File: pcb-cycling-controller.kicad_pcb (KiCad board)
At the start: 4 copper layers, 54.6 x 40.6 mm, 85 parts, among them J1 Conn_01x02, J2 USB_C_Receptacle_USB2.0_16P, J3 Conn_01x06, J6 LED1, J7 LED1, Q1 SI2301CDS-T1-GE3-ES, Q2 SI2301CDS-T1-GE3-ES, SW1 SS12F44G4, U1 ESP32-S3-WROOM-1, U2 LMV321, U3 L7805, U4 MT3410LB, U5 74AHCT125, U7 DS1307Z+, U8 LMV321, Y2 32.768 kHz

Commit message: Add details to the design
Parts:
- removed C32: 0.1uF, Capacitor_SMD:C_0402_1005Metric
- removed R14, R15, R37: 0, Resistor_SMD:R_0603_1608Metric
- removed R32: 11k, Resistor_SMD:R_0603_1608Metric
- removed R33: 3.3k, Resistor_SMD:R_0603_1608Metric
- removed U8: LMV321, Package_TO_SOT_SMD:SOT-23-5_HandSoldering
- added C34: 0.1uF, Capacitor_SMD:C_0402_1005Metric, B.Cu at (70.1, 94.7)
- added C35: 0.1uF, Capacitor_SMD:C_0402_1005Metric, F.Cu at (82.8, 90.4)
- added C36: 0.1uF, Capacitor_SMD:C_0402_1005Metric, F.Cu at (84.6, 90.4)
- added C9: 1uF, Capacitor_SMD:C_0603_1608Metric, B.Cu at (75.7, 84.8)
- added D8: A7, Diode_SMD:D_SOD-123F, F.Cu at (75.9, 77.0)
- added J8: SENSOR, Connector_Molex:Molex_KK-254_AE-6410-03A_1x03_P2.54mm_Vertical, F.Cu at (63.2, 82.5)
- added J9: OLED, Connector_PinSocket_2.54mm:PinSocket_1x04_P2.54mm_Vertical, F.Cu at (78.0, 105.4)
- added R38: 0, Resistor_SMD:R_0603_1608Metric, F.Cu at (67.6, 95.5)
- added R39: 0, Resistor_SMD:R_0603_1608Metric, B.Cu at (70.6, 96.8)
- added R40: 0, Resistor_SMD:R_0603_1608Metric, F.Cu at (67.6, 98.6)
- added R5: 10k, Resistor_SMD:R_0603_1608Metric, F.Cu at (82.8, 87.9)
- added R6: 10k, Resistor_SMD:R_0603_1608Metric, F.Cu at (84.6, 87.9)
- added SW2: BTN1, jlcpcb:SW-SMD_4P-L5.1-W5.1-P3.70-LS6.5-TL_H1.5, F.Cu at (78.2, 90.7)
- added SW3: BTN2, jlcpcb:SW-SMD_4P-L5.1-W5.1-P3.70-LS6.5-TL_H1.5, F.Cu at (89.2, 90.7)
- added U6: AMS1117-5.0, Package_TO_SOT_SMD:SOT-223-3_TabPin2, B.Cu at (70.6, 88.1)
- C33: value 0.1uF -> 22uF 10V; footprint Capacitor_SMD:C_0402_1005Metric -> Capacitor_SMD:C_0603_1608Metric; moved to B.Cu
- J1: value Conn_01x02 -> Power; footprint Connector_PinHeader_2.54mm:PinHeader_1x02_P2.54mm_Vertical -> Connector_Molex:Molex_KK-254_AE-6410-02A_1x02_P2.54mm_Vertical
- J2: value USB_C_Receptacle_USB2.0_16P -> USB
- J3: value Conn_01x06 -> PROG
- J6: footprint Connector_PinHeader_2.54mm:PinHeader_1x05_P2.54mm_Vertical -> Connector_Molex:Molex_KK-254_AE-6410-04A_1x04_P2.54mm_Vertical
- J7: value LED1 -> LED2; footprint Connector_PinHeader_2.54mm:PinHeader_1x05_P2.54mm_Vertical -> Connector_Molex:Molex_KK-254_AE-6410-04A_1x04_P2.54mm_Vertical
- U3: value L7805 -> AMS1117-5.0; footprint Package_TO_SOT_SMD:TO-263-2 -> Package_TO_SOT_SMD:SOT-223-3_TabPin2
- U5: footprint Package_SO:SOIC-14W_7.5x9mm_P1.27mm -> Package_SO:TSSOP-14_4.4x5mm_P0.65mm
- moved C28 72.8 mm to (82.3, 100.1), turned to -90 degrees
- moved FID1 70.9 mm to (107.4, 69.6)
- moved R31 70.1 mm to (70.4, 81.0)
- moved R18 69.6 mm to (82.3, 102.9)
- moved R12 68.3 mm to (86.4, 102.9), turned to 180 degrees
- moved R19 67.5 mm to (80.8, 100.1), turned to 90 degrees
- moved C31 67.0 mm to (73.9, 77.0), turned to 90 degrees
- moved C33 65.5 mm to (69.8, 93.5)
- moved U2 62.7 mm to (70.9, 78.4)
- moved R20 62.1 mm to (67.6, 78.5), turned to 90 degrees
- moved C30 62.1 mm to (73.7, 82.3), turned to 180 degrees
- moved C29 62.0 mm to (83.6, 99.5), turned to -90 degrees
- moved R13 61.8 mm to (70.4, 75.7)
- moved R21 61.0 mm to (73.4, 81.0)
- moved D7 60.1 mm to (79.0, 100.1), turned to -90 degrees
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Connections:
- net /BUCK_VIN renamed BUCK_VIN
- C14 pad 2: +5V -> Net-(U3-VO)
- C15 pad 1: +5V -> Net-(U3-VO)
- C30 pad 1: SENSOR_1_FILT -> SENSOR_FILT
- C33 pad 1: SENSOR_1_FILT -> GND
- C33 pad 2: GND -> Net-(U6-VO)
- J6 pad 1: VLED -> VLED1
- J6 pad 4: SENSOR_1 -> GND
- J7 pad 1: VLED -> VLED2
- J7 pad 4: SENSOR_2 -> GND
- R20 pad 1: SENSOR_1 -> Net-(J8-Pin_2)
- R21 pad 1: Net-(U2--) -> Net-(R21-Pad1)
- R21 pad 2: SENSOR_1_FILT -> SENSOR_FILT
- R31 pad 1: SENSOR_1 -> Net-(U2--)
- R31 pad 2: Net-(U8-+) -> Net-(R21-Pad1)
- U1 pad 10: STATUS -> unconnected-(U1-IO17-Pad10)
- U1 pad 15: unconnected-(U1-IO3-Pad15) -> BATT_VOLTAGE
- U1 pad 16: unconnected-(U1-IO46-Pad16) -> STATUS
- U1 pad 17: unconnected-(U1-IO9-Pad17) -> SENSOR_FILT
- U1 pad 18: unconnected-(U1-IO10-Pad18) -> BTN1
- U1 pad 19: unconnected-(U1-IO11-Pad19) -> BTN2
- U1 pad 25: unconnected-(U1-IO48-Pad25) -> I2C_SDA
- U1 pad 26: unconnected-(U1-IO45-Pad26) -> I2C_SCL
- U1 pad 31: STRIP1_D -> STRIP2_C
- U1 pad 32: STRIP1_C -> STRIP2_D
- U1 pad 33: STRIP2_D -> STRIP1_C
- U1 pad 34: STRIP2_C -> STRIP1_D
- U1 pad 39: BATT_VOLTAGE -> unconnected-(U1-IO1-Pad39)
- U1 pad 4: I2C_SDA -> unconnected-(U1-IO4-Pad4)
- U1 pad 5: I2C_SCL -> unconnected-(U1-IO5-Pad5)
- U1 pad 6: SENSOR1_FILT -> unconnected-(U1-IO6-Pad6)
- U1 pad 7: SENSOR2_FILT -> unconnected-(U1-IO7-Pad7)
- U2 pad 4: Net-(U2--) -> Net-(R21-Pad1)
- U3 pad 1: VBAT_SW -> GND
- U3 pad 2: GND -> Net-(U3-VO)
- U3 pad 3: +5V -> VBAT_SW
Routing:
- net ~{RST}: track 0.00 -> 45.2 mm, vias 0 -> 1
- net VBAT_PROT: track 11.4 -> 54.8 mm, vias 0 -> 1
- net GND: track 35.4 -> 73.2 mm, vias 22 -> 68
- net STRIP1_C: track 0.00 -> 35.9 mm, vias 0 -> 2
- net STRIP2_D: track 0.00 -> 35.3 mm, vias 0 -> 2
- net STRIP1_D: track 0.00 -> 35.2 mm, vias 0 -> 2
- net Net-(D8-A): track 0.00 -> 30.3 mm, vias 0 -> 3
- net STRIP2_C: track 0.00 -> 30.1 mm, vias 0 -> 2
- net +3V3: track 5.55 -> 28.1 mm, vias 0 -> 19
- net SENSOR_FILT: track 0.00 -> 22.5 mm, vias 0 -> 2
- net BTN1: track 0.00 -> 21.2 mm
- net Net-(J2-SHIELD): track 0.00 -> 19.0 mm
- net I2C_SCL: track 0.00 -> 16.9 mm, vias 0 -> 2
- net I2C_SDA: track 0.00 -> 16.4 mm
- net VLED2: track 0.00 -> 15.4 mm, vias 0 -> 2
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- added copper zone on In2.Cu, net +3V3
- added copper zone on F.Cu, net GND
- added copper zone on In2.Cu, net VBAT_SW
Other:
- board text removed: "SCL"
- board text removed: "SDA"

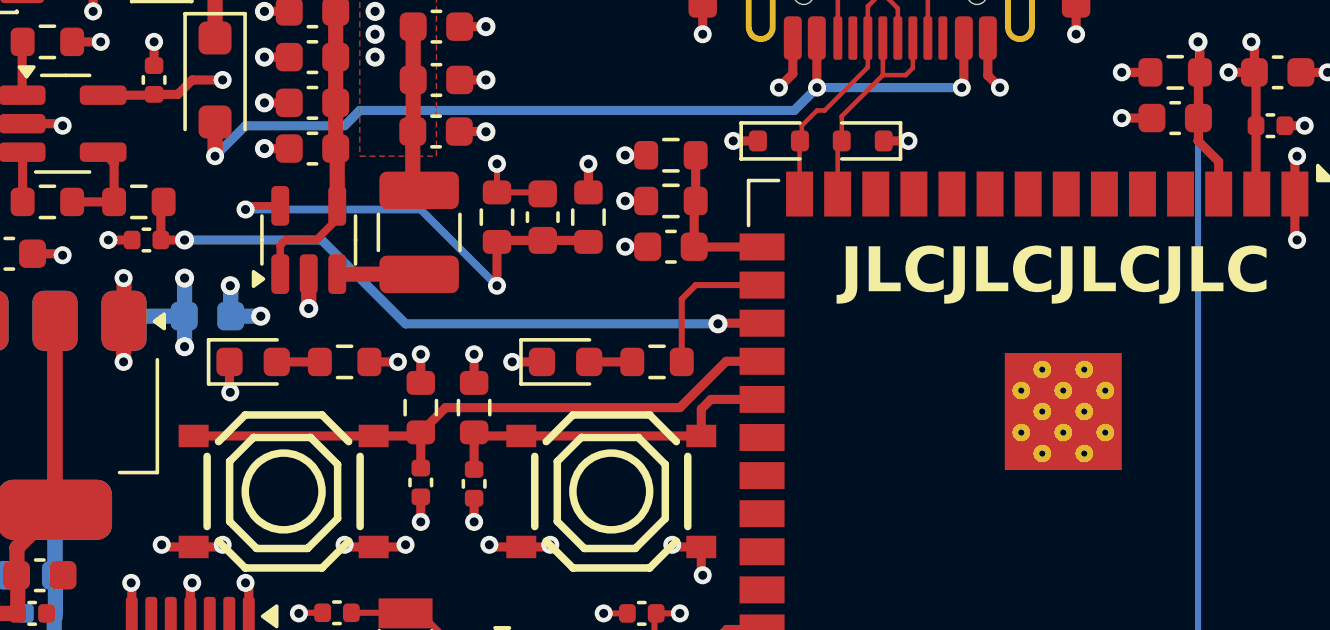
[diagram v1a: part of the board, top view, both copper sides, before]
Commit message: Update ADC pin assignments due to issue #4
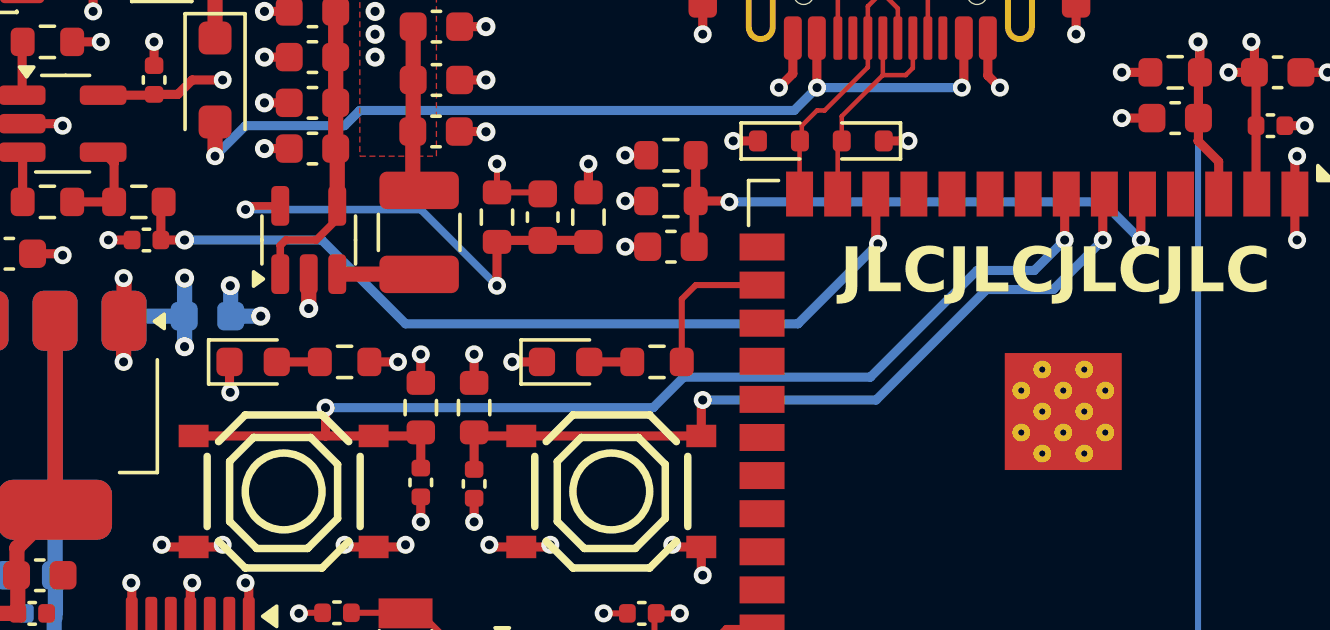
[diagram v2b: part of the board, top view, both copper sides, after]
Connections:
- U1 pad 12: unconnected-(U1-IO8-Pad12) -> SENSOR_FILT
- U1 pad 15: BATT_VOLTAGE -> unconnected-(U1-IO3-Pad15)
- U1 pad 17: SENSOR_FILT -> unconnected-(U1-IO9-Pad17)
- U1 pad 18: BTN1 -> unconnected-(U1-IO10-Pad18)
- U1 pad 19: BTN2 -> unconnected-(U1-IO11-Pad19)
- U1 pad 5: unconnected-(U1-IO5-Pad5) -> BATT_VOLTAGE
- U1 pad 6: unconnected-(U1-IO6-Pad6) -> BTN2
- U1 pad 7: unconnected-(U1-IO7-Pad7) -> BTN1
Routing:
- net BTN1: track 21.2 -> 38.3 mm, vias 0 -> 2
- net BTN2: track 11.9 -> 27.2 mm, vias 0 -> 2
- net BATT_VOLTAGE: track 5.42 -> 20.1 mm, vias 0 -> 2
- net SENSOR_FILT: track 22.5 -> 29.2 mm

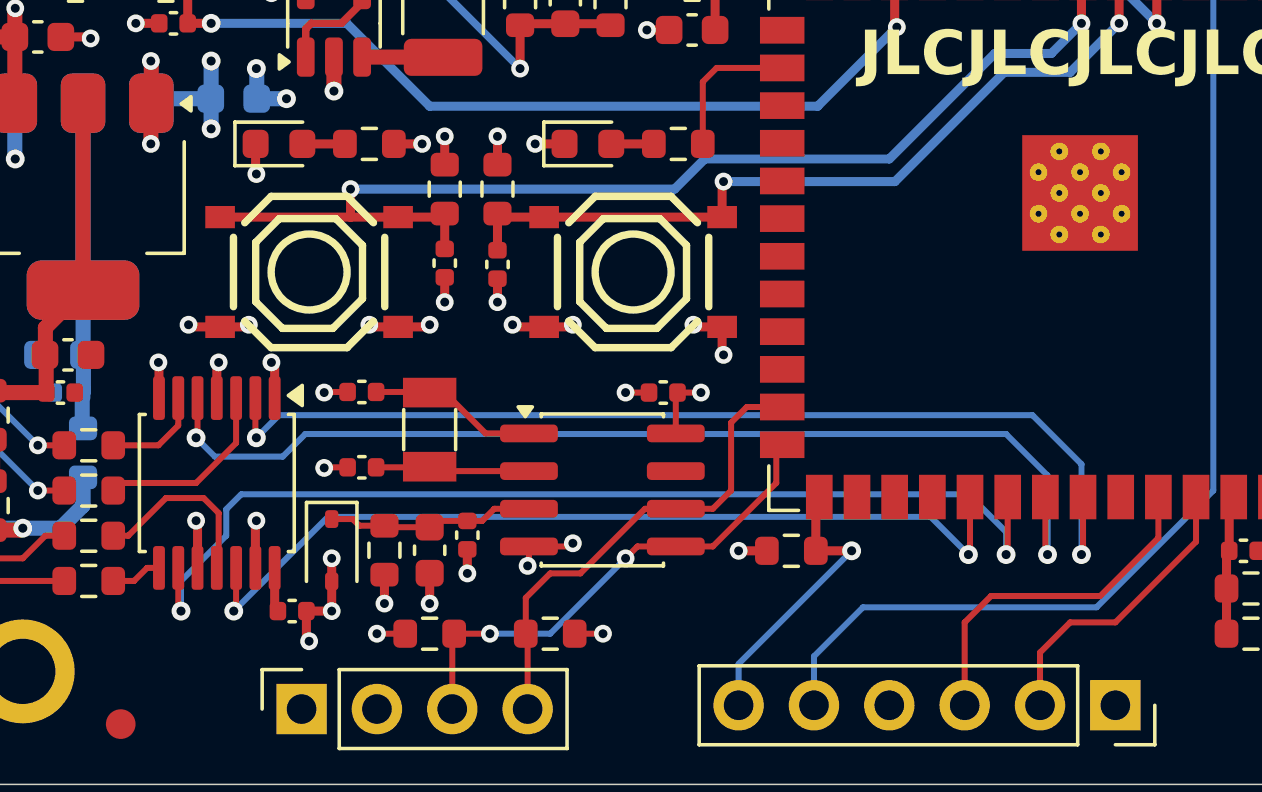
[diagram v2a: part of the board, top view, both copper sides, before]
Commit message: Update LED strip pinout per #1
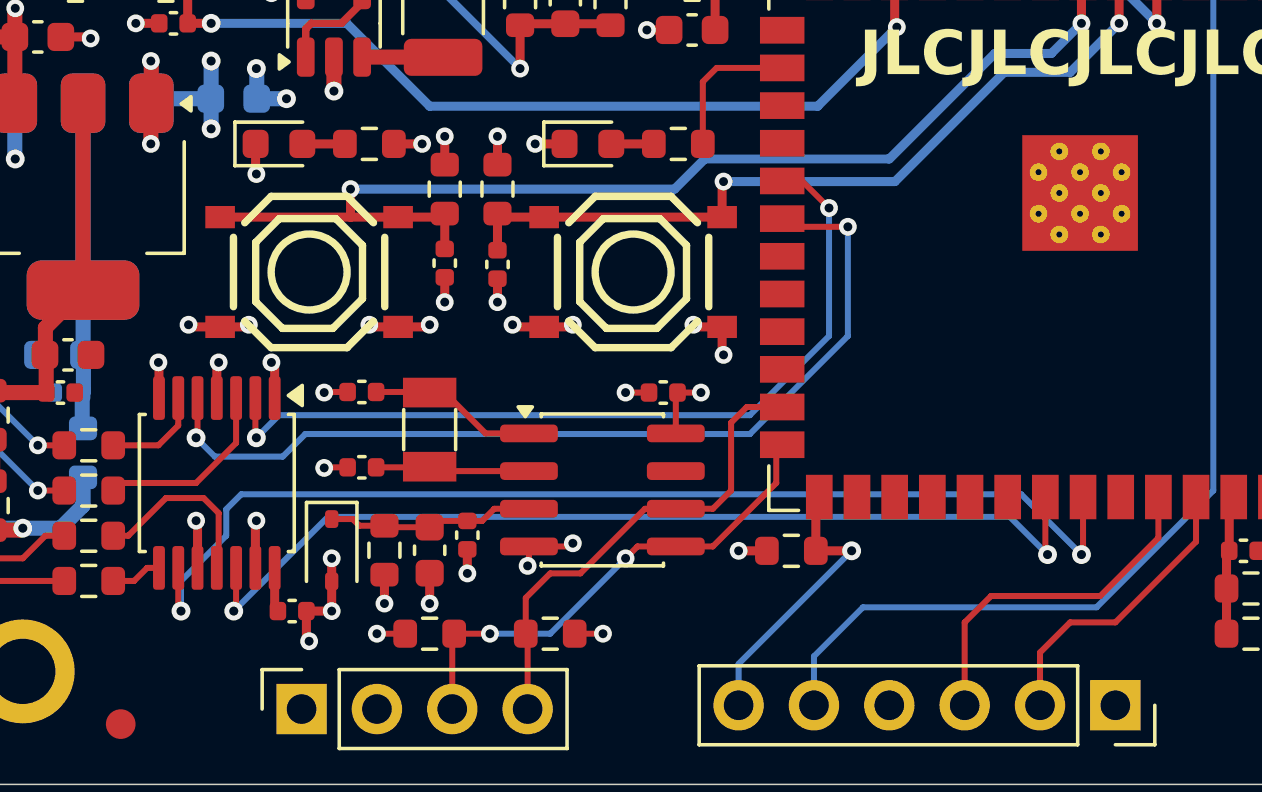
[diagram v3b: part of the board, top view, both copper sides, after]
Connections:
- U1 pad 19: unconnected-(U1-IO11-Pad19) -> STRIP1_D
- U1 pad 20: unconnected-(U1-IO12-Pad20) -> STRIP1_C
- U1 pad 31: STRIP2_C -> unconnected-(U1-IO38-Pad31)
- U1 pad 32: STRIP2_D -> unconnected-(U1-IO39-Pad32)
- U1 pad 33: STRIP1_C -> STRIP2_C
- U1 pad 34: STRIP1_D -> STRIP2_D
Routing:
- net STRIP1_D: track 35.2 -> 28.3 mm
- net STRIP1_C: track 35.9 -> 31.3 mm
- net STRIP2_C: track 30.1 -> 32.7 mm
- net STRIP2_D: track 35.3 -> 37.4 mm
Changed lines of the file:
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@@
 			(size 1.5 0.9)
 			(layers "F.Cu" "F.Mask" "F.Paste")
-			(net "unconnected-(U1-IO11-Pad19)")
+			(net "STRIP1_D")
 			(pinfunction "IO11_19")
 			(pintype "bidirectional")
@@
 			(size 1.5 0.9)
 			(layers "F.Cu" "F.Mask" "F.Paste")
-			(net "unconnected-(U1-IO12-Pad20)")
+			(net "STRIP1_C")
 			(pinfunction "IO12_20")
 			(pintype "bidirectional")
@@
 			(size 1.5 0.9)
 			(layers "F.Cu" "F.Mask" "F.Paste")
-			(net "STRIP2_C")
+			(net "unconnected-(U1-IO38-Pad31)")
 			(pinfunction "IO38_31")
 			(pintype "bidirectional")
@@
 			(size 1.5 0.9)
 			(layers "F.Cu" "F.Mask" "F.Paste")
-			(net "STRIP2_D")
+			(net "unconnected-(U1-IO39-Pad32)")
 			(pinfunction "IO39_32")
 			(pintype "bidirectional")
@@
 			(size 1.5 0.9)
 			(layers "F.Cu" "F.Mask" "F.Paste")
-			(net "STRIP1_C")
+			(net "STRIP2_C")
 			(pinfunction "IO40_33")
 			(pintype "bidirectional")
@@
 			(size 1.5 0.9)
 			(layers "F.Cu" "F.Mask" "F.Paste")
-			(net "STRIP1_D")
+			(net "STRIP2_D")
 			(pinfunction "IO41_34")
 			(pintype "bidirectional")
@@
 	)
 	(segment
-		(start 104.32 98.264)
-		(end 104.32 100.15)
+		(start 76.421 94.9275)
+		(end 76.421 96.233)
 		(width 0.2032)
 		(layer "F.Cu")
@@
 	)
 	(segment
-		(start 76.421 94.9275)
-		(end 76.421 96.233)
-		(width 0.2032)
+		(start 95.758 88.519)
+		(end 94.848 87.609)
+		(width 0.2)
 		(layer "F.Cu")
 		(net "STRIP1_D")
 	)
 	(segment
-		(start 104.32 100.15)
-		(end 104.267 100.203)
-		(width 0.2032)
+		(start 94.848 87.609)
+		(end 94.18 87.609)
+		(width 0.2)
 		(layer "F.Cu")
 		(net "STRIP1_D")
@@
 	)
 	(via
-		(at 104.267 100.203)
-		(size 0.635)
-		(drill 0.3048)
+		(at 95.758 88.519)
+		(size 0.6)
+		(drill 0.3)
 		(layers "F.Cu" "B.Cu")
 		(net "STRIP1_D")
@@
 	)
 	(segment
-		(start 104.267 97.155)
-		(end 102.616 95.504)
+		(start 93.091 95.504)
+		(end 95.758 92.837)
 		(width 0.2032)
 		(layer "B.Cu")
@@
 	)
 	(segment
-		(start 102.616 95.504)
+		(start 93.091 95.504)
 		(end 77.216 95.504)
 		(width 0.2032)
@@
 	)
 	(segment
-		(start 104.267 100.203)
-		(end 104.267 97.155)
+		(start 95.758 92.837)
+		(end 95.758 88.519)
 		(width 0.2032)
 		(layer "B.Cu")
@@
 	)
 	(segment
-		(start 103.05 98.264)
-		(end 103.05 100.129)
+		(start 96.393 89.154)
+		(end 94.455 89.154)
 		(width 0.2032)
 		(layer "F.Cu")
@@
 	)
 	(segment
-		(start 103.05 100.129)
-		(end 103.124 100.203)
+		(start 94.455 89.154)
+		(end 94.18 88.879)
 		(width 0.2032)
 		(layer "F.Cu")
@@
 	)
 	(via
-		(at 103.124 100.203)
-		(size 0.635)
-		(drill 0.3048)
+		(at 96.393 89.154)
+		(size 0.6)
+		(drill 0.3)
 		(layers "F.Cu" "B.Cu")
 		(net "STRIP1_C")
 	)
 	(segment
-		(start 78.105 96.139)
-		(end 77.343 96.901)
+		(start 93.091 96.139)
+		(end 96.393 92.837)
 		(width 0.2032)
 		(layer "B.Cu")
@@
 	)
 	(segment
-		(start 75.057 96.901)
-		(end 74.422 96.266)
+		(start 96.393 92.837)
+		(end 96.393 89.154)
 		(width 0.2032)
 		(layer "B.Cu")
@@
 	)
 	(segment
-		(start 101.727 96.139)
-		(end 80.645 96.139)
+		(start 78.105 96.139)
+		(end 77.343 96.901)
 		(width 0.2032)
 		(layer "B.Cu")
@@
 	)
 	(segment
-		(start 103.124 100.203)
-		(end 103.124 97.536)
+		(start 75.057 96.901)
+		(end 74.422 96.266)
 		(width 0.2032)
 		(layer "B.Cu")
@@
 	)
 	(segment
-		(start 103.124 97.536)
-		(end 101.727 96.139)
+		(start 77.343 96.901)
+		(end 75.057 96.901)
 		(width 0.2032)
 		(layer "B.Cu")
@@
 	)
 	(segment
-		(start 77.343 96.901)
-		(end 75.057 96.901)
+		(start 93.091 96.139)
+		(end 80.645 96.139)
 		(width 0.2032)
 		(layer "B.Cu")
@@
 	)
 	(segment
-		(start 73.821 102.015)
-		(end 73.914 102.108)
+		(start 104.32 98.264)
+		(end 104.32 100.15)
 		(width 0.2032)
 		(layer "F.Cu")
@@
 	)
 	(segment
-		(start 73.821 100.6525)
-		(end 73.821 102.015)
+		(start 73.821 102.015)
+		(end 73.914 102.108)
 		(width 0.2032)
 		(layer "F.Cu")
@@
 	)
 	(segment
-		(start 101.78 100.15)
-		(end 101.727 100.203)
+		(start 73.821 100.6525)
+		(end 73.821 102.015)
 		(width 0.2032)
 		(layer "F.Cu")
@@
 	)
 	(segment
-		(start 101.78 98.264)
-		(end 101.78 100.15)
+		(start 104.32 100.15)
+		(end 104.267 100.203)
 		(width 0.2032)
 		(layer "F.Cu")
@@
 	)
 	(via
-		(at 101.727 100.203)
+		(at 104.267 100.203)
 		(size 0.635)
 		(drill 0.3048)
@@
 	)
 	(segment
-		(start 75.438 98.679)
-		(end 75.438 99.568)
+		(start 73.914 102.108)
+		(end 73.914 101.092)
 		(width 0.2032)
 		(layer "B.Cu")
@@
 	)
 	(segment
-		(start 101.727 99.441)
-		(end 100.457 98.171)
+		(start 75.946 98.171)
+		(end 102.235 98.171)
 		(width 0.2032)
 		(layer "B.Cu")
@@
 	)
 	(segment
-		(start 73.914 101.092)
-		(end 73.914 102.108)
+		(start 75.438 98.679)
+		(end 75.946 98.171)
 		(width 0.2032)
 		(layer "B.Cu")
@@
 	)
 	(segment
-		(start 101.727 100.203)
-		(end 101.727 99.441)
+		(start 73.914 101.092)
+		(end 75.438 99.568)
 		(width 0.2032)
 		(layer "B.Cu")
@@
 	(segment
 		(start 75.438 99.568)
-		(end 73.914 101.092)
-		(width 0.2032)
-		(layer "B.Cu")
-		(net "STRIP2_D")
-	)
-	(segment
-		(start 100.457 98.171)
-		(end 75.946 98.171)
+		(end 75.438 98.679)
 		(width 0.2032)
 		(layer "B.Cu")
@@
 	)
 	(segment
-		(start 75.946 98.171)
-		(end 75.438 98.679)
+		(start 102.235 98.171)
+		(end 104.267 100.203)
 		(width 0.2032)
 		(layer "B.Cu")
@@
 	)
 	(segment
-		(start 100.51 100.15)
-		(end 100.457 100.203)
+		(start 103.05 98.264)
+		(end 103.05 100.129)
 		(width 0.2032)
 		(layer "F.Cu")
@@
 	)
 	(segment
-		(start 75.771 102.029)
-		(end 75.692 102.108)
+		(start 103.05 100.129)
+		(end 103.124 100.203)
 		(width 0.2032)
 		(layer "F.Cu")
@@
 	)
 	(segment
-		(start 100.51 98.264)
-		(end 100.51 100.15)
+		(start 75.771 102.029)
+		(end 75.692 102.108)
 		(width 0.2032)
 		(layer "F.Cu")
@@
 	)
 	(via
-		(at 100.457 100.203)
+		(at 75.692 102.108)
 		(size 0.635)
 		(drill 0.3048)
@@
 	)
 	(via
-		(at 75.692 102.108)
+		(at 103.124 100.203)
 		(size 0.635)
 		(drill 0.3048)
@@
 	)
 	(segment
-		(start 78.867 98.933)
-		(end 99.187 98.933)
+		(start 101.854 98.933)
+		(end 103.124 100.203)
 		(width 0.2032)
 		(layer "B.Cu")
@@
 	)
 	(segment
-		(start 75.692 102.108)
-		(end 78.867 98.933)
+		(start 78.867 98.933)
+		(end 101.854 98.933)
 		(width 0.2032)
 		(layer "B.Cu")
@@
 	)
 	(segment
-		(start 99.187 98.933)
-		(end 100.457 100.203)
+		(start 75.692 102.108)
+		(end 78.867 98.933)
 		(width 0.2032)
 		(layer "B.Cu")
